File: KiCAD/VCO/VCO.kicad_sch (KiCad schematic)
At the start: 34 parts, among them Q1 NPN, T1 PNP, T2 NPN, U1 4069, U2 4069, U3 4069

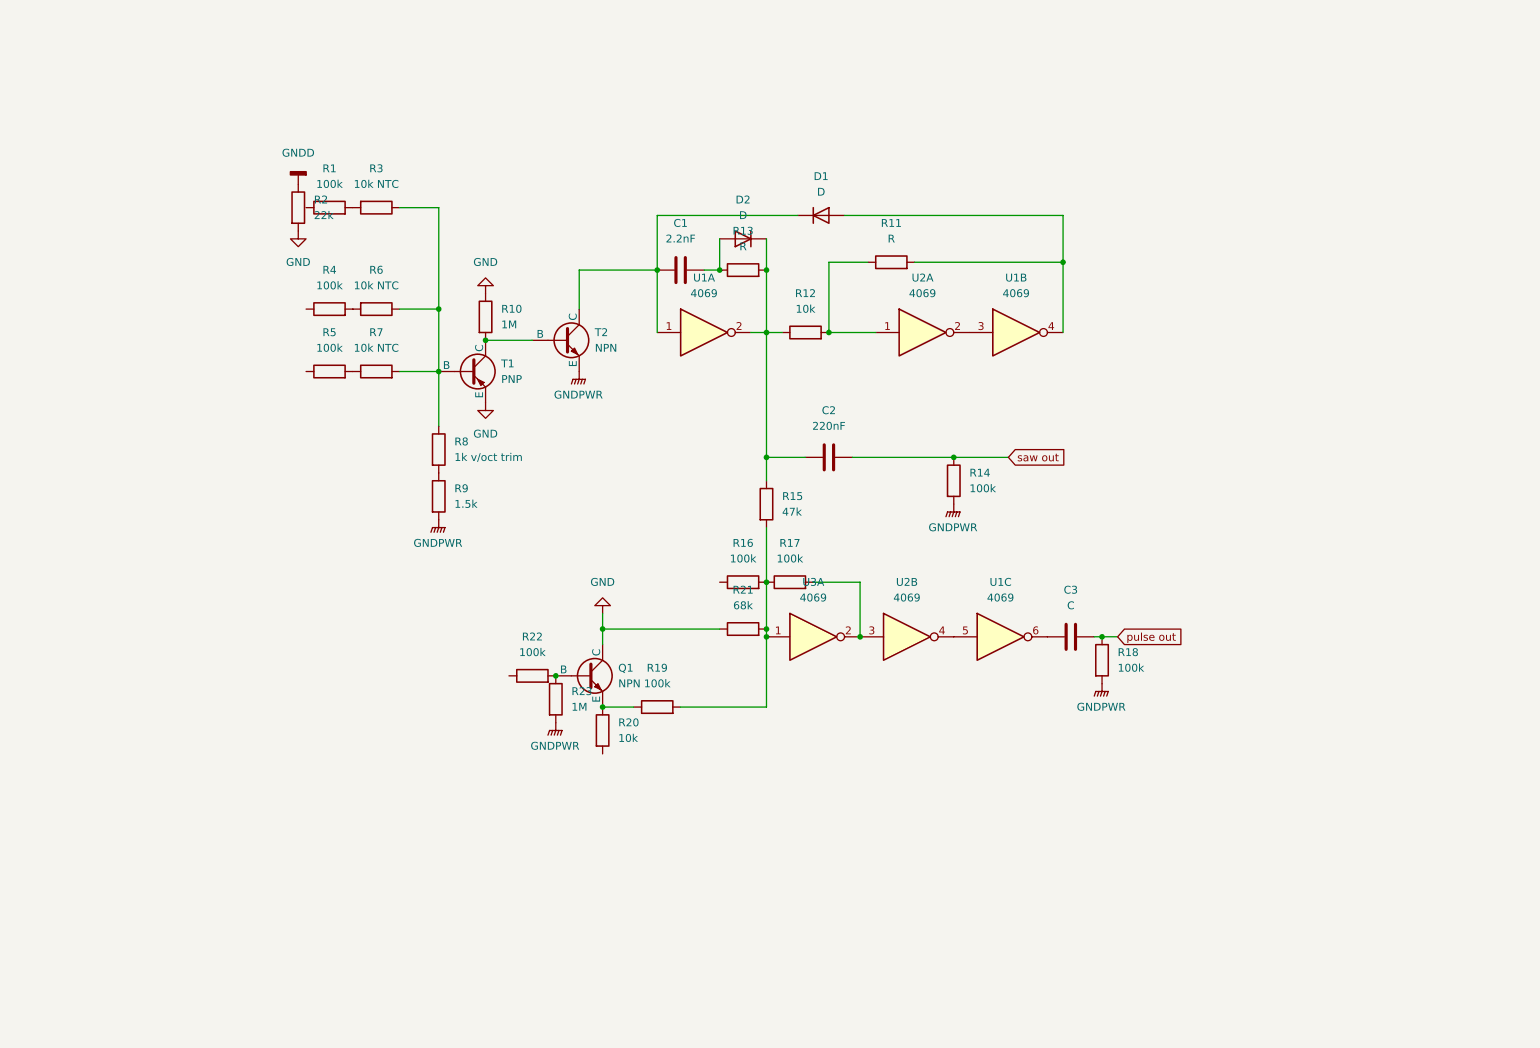
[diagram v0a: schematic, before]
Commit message: Add footprint library components.
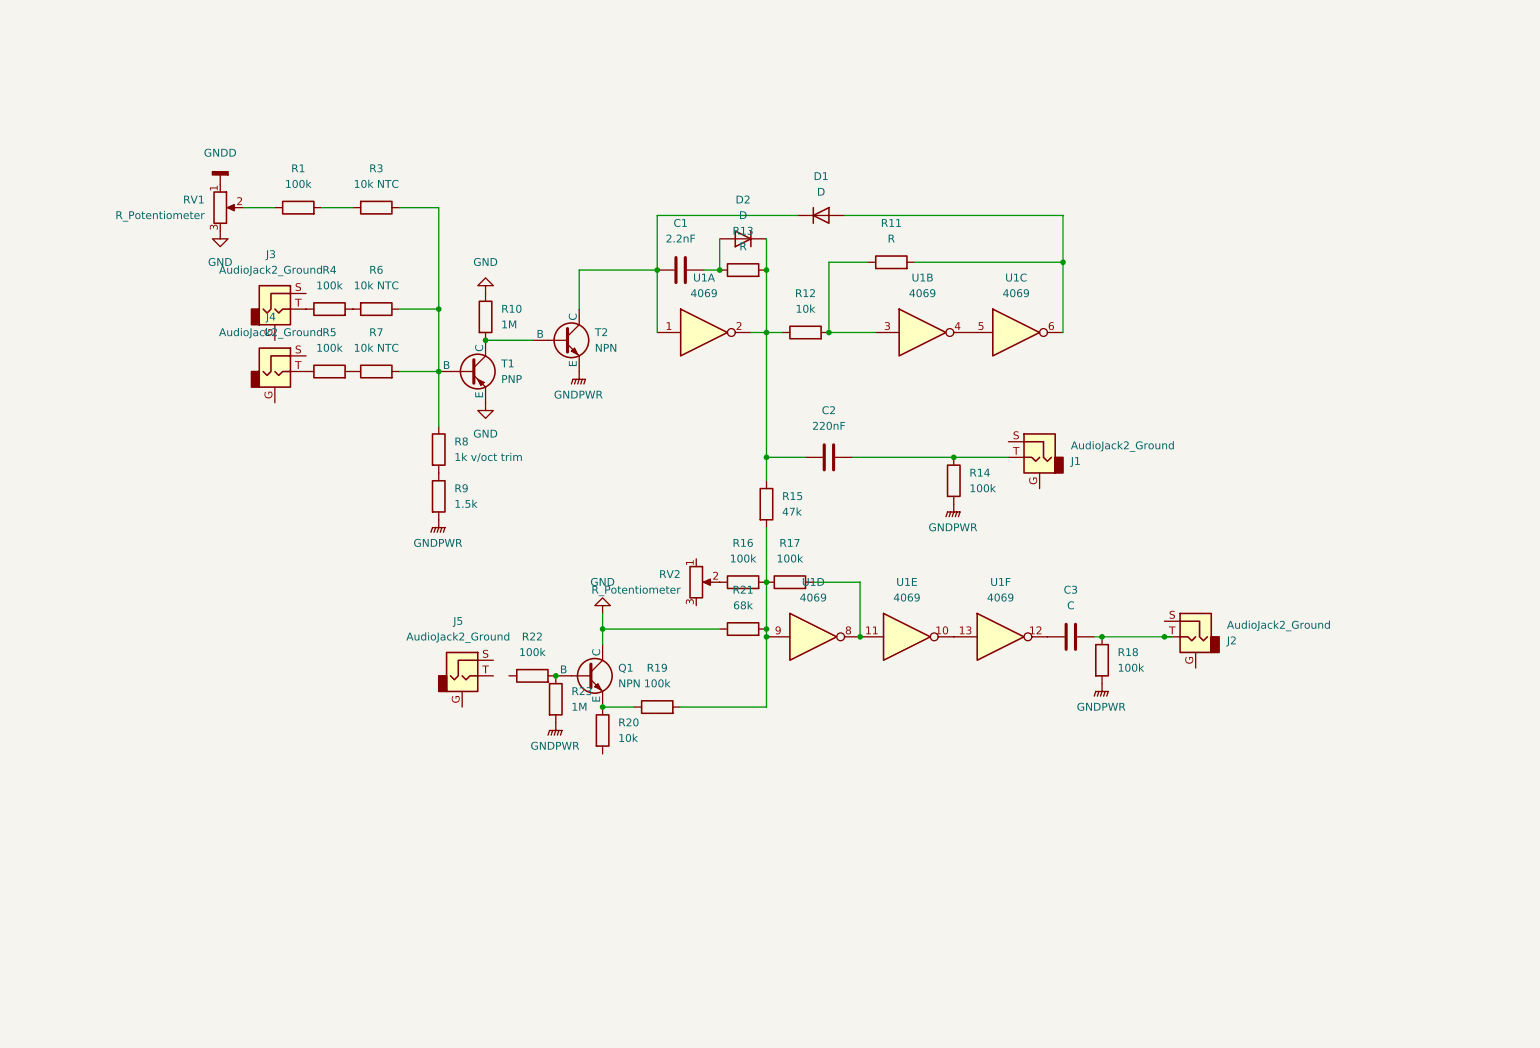
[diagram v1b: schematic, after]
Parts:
- removed R2: 22k, symbol Device:R
- added J1, J2, J3, J4, J5: AudioJack2_Ground, HackSynth:Jack_3.5mm, symbol HackSynth:AudioJack2_Ground
- added RV1, RV2: R_Potentiometer, HackSynth:Potentiometer_Alps_RK09K_Horizontal, symbol HackSynth:R_Potentiometer
- C1, C2, C3: footprint (none) -> Capacitor_THT:C_Disc_D5.0mm_W2.5mm_P2.50mm
- D1, D2: footprint (none) -> Diode_THT:D_5KPW_P12.70mm_Horizontal
- Q1: footprint (none) -> Package_TO_SOT_THT:TO-92L_Inline
- R1, R10, R11, R12, R13, R14, R15, R16, R17, R18, R19, R20, R21, R22, R23, R3, R4, R5, R6, R7, R8, R9: footprint (none) -> Resistor_THT:R_Axial_DIN0207_L6.3mm_D2.5mm_P7.62mm_Horizontal
- T1, T2: footprint (none) -> Package_TO_SOT_THT:TO-92_Inline
- U1: renamed from U3; footprint (none) -> Package_DIP:DIP-4_W7.62mm_LongPads
- U1: renamed from U2; footprint (none) -> Package_DIP:DIP-4_W7.62mm_LongPads
- U1: footprint (none) -> Package_DIP:DIP-4_W7.62mm_LongPads
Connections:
- net GND: now also RV1.3
- net GNDD: now also RV1.1
- net at R16.1: now also RV2.2
- net at R15.2, R16.2, R17.1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: now also U1.9; no longer U1.1
- net at C3.1: now also U1.12; no longer U1.6
- net at R5.1: now also J4.T
- net at D1.2 (A), R11.2: now also U1.6; no longer U1.4
- net at R11.1, R12.2: now also U1.3; no longer U1.1
- net at R4.1: now also J3.T
- net at R1.1: now also RV1.2
- net pulse out: no longer names the net of C3.2, R18.1
- net pulse out: now also J2.T
- net saw out: no longer names the net of C2.2, R14.1
- net saw out: now also J1.T
- new net: R17.2, U1.11, U1.8
- new net: U1.10, U1.13
- new net: U1.4, U1.5
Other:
- moved on the sheet: R1

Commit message: VCO and Power updates
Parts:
- removed R8: 1k v/oct trim, Resistor_THT:R_Axial_DIN0207_L6.3mm_D2.5mm_P7.62mm_Horizontal, symbol Device:R
- added RV3: R_Potentiometer_Trim 1k, symbol Device:R_Potentiometer_Trim
- C3: value C -> 220nF
- renumbered J3 to J1, J4 to J2, J5 to J3, J1 to J4, J2 to J5
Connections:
- net GNDD is gone; now on net GND: RV1.1
- net GNDPWR is gone; now on net GND: R14.2, R18.2, R23.2, R9.2, T2.3 (E)
- net GND: now also J1.G, J2.G, J3.G, J4.G, J5.G, RV2.3; no longer Q1.1 (C), R10.1, R21.1, RV1.3, T1.3 (E)
- net VDD: now reaches RV2.1
- net VDD: now also Q1.1 (C), R10.1, R21.1
- net at J3.T: now also R22.1
- net at R3.1, R6.1, R7.2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: now also RV3.1
- net at R9.1: now also RV3.2, RV3.3
- net VSS: now reaches R20.2
- net VSS: now also RV1.3, T1.3 (E)
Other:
- note added: "CV IN 1"
- note added: "CV IN 2"
- note added: "PULSE OUT"
- note added: "PW ADJUST"
- note added: "PWM"
- note added: "SAW OUT"
- note added: "V/OCT TRIM"
- moved on the sheet: C1, C2, C3, D1, D2, J1, J2, J3, J4, J5, Q1, R1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

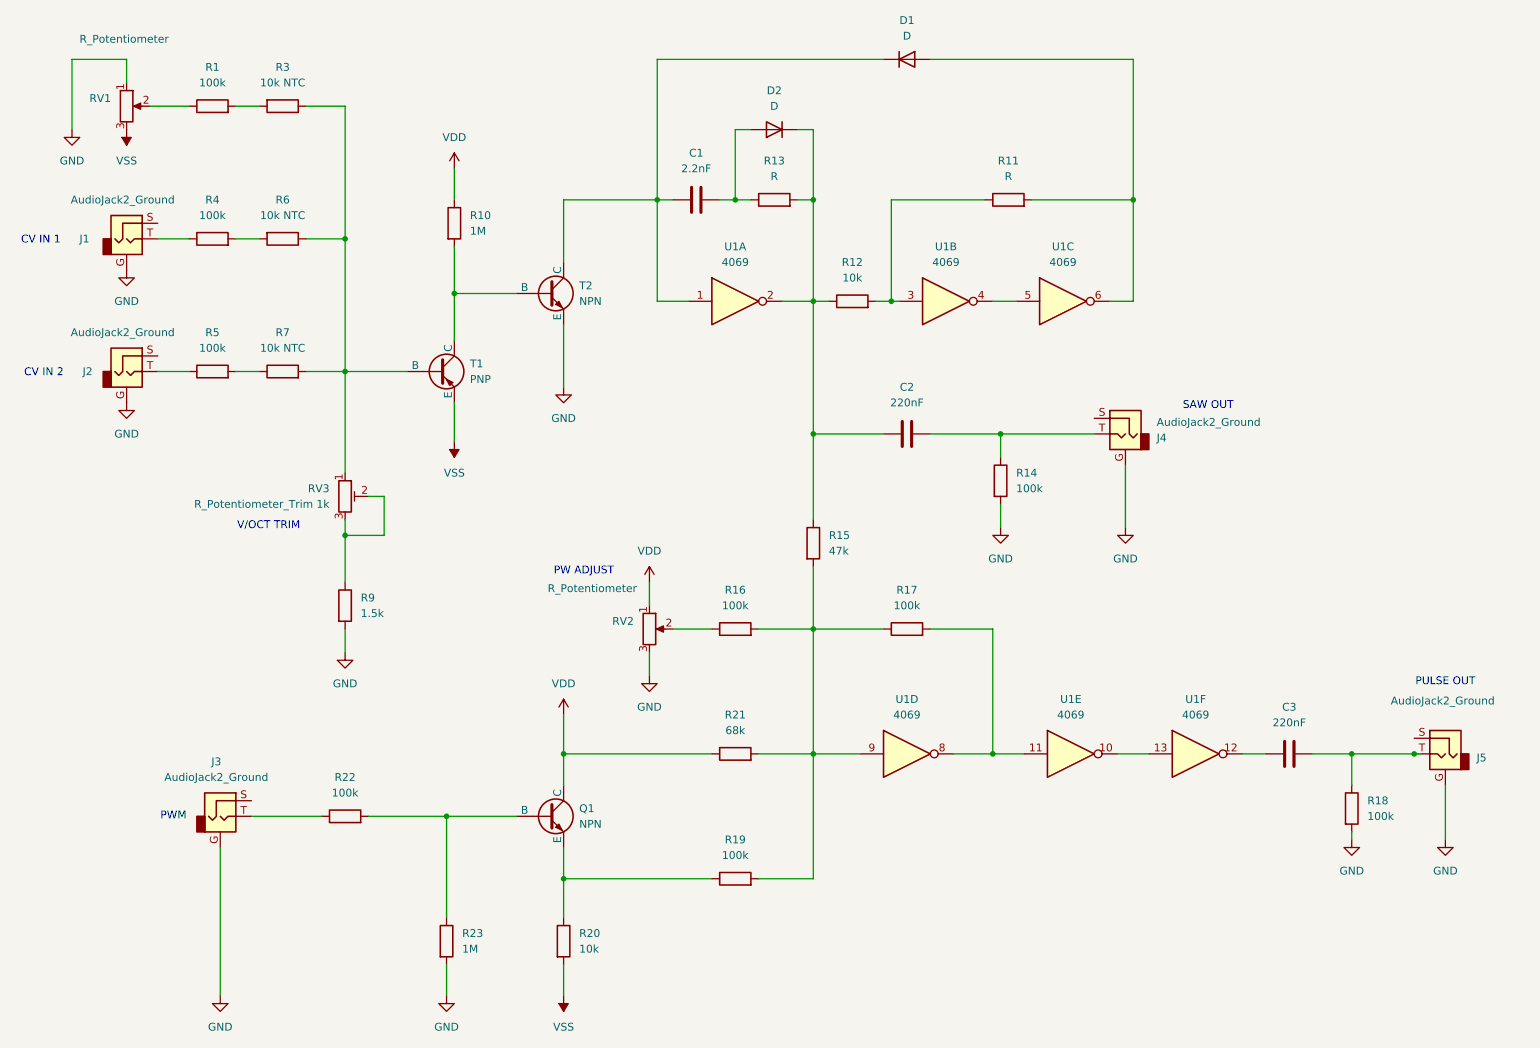
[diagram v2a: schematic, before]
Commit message: Power Schematic and Libraries
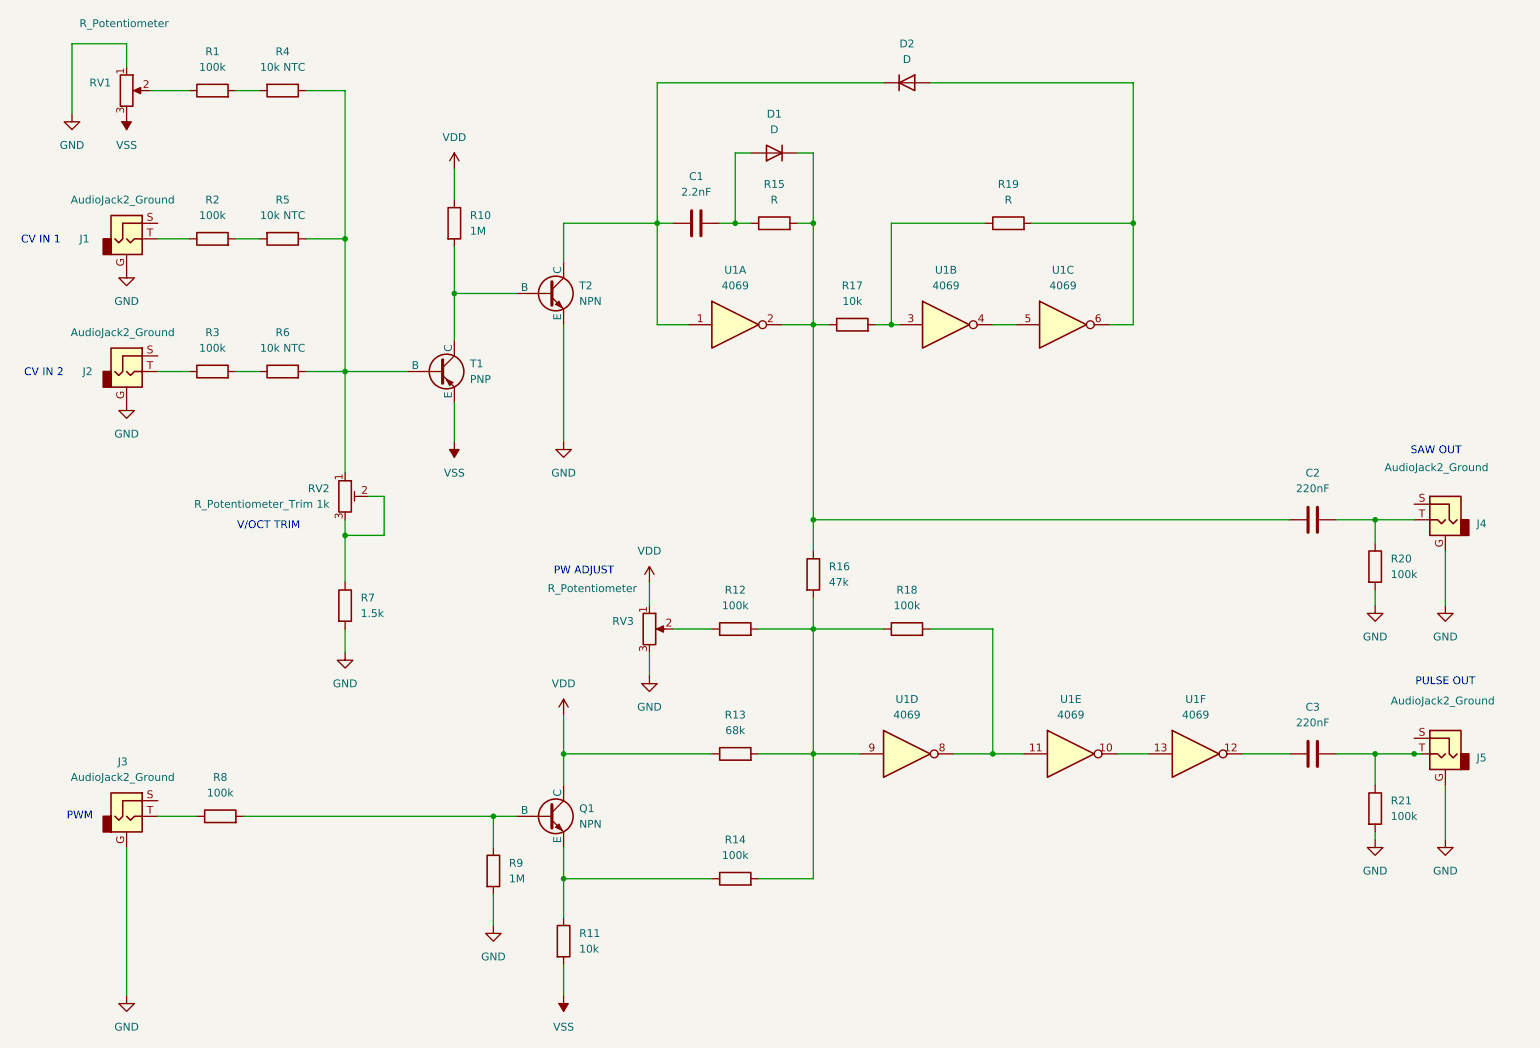
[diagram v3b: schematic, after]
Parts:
- D1: renamed from D2; footprint Diode_THT:D_5KPW_P12.70mm_Horizontal -> Diode_THT:D_A-405_P7.62mm_Horizontal
- D2: renamed from D1; footprint Diode_THT:D_5KPW_P12.70mm_Horizontal -> Diode_THT:D_A-405_P7.62mm_Horizontal
- U1: footprint Package_DIP:DIP-4_W7.62mm_LongPads -> Package_DIP:DIP-14_W7.62mm_LongPads
- renumbered R20 to R11, R16 to R12, R21 to R13, R19 to R14, R13 to R15, R15 to R16, R12 to R17, R17 to R18, R11 to R19, R4 to R2, R14 to R20, R18 to R21, R5 to R3, R3 to R4, R6 to R5, R7 to R6, R9 to R7, R22 to R8, R23 to R9, RV3 to RV2, RV2 to RV3
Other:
- moved on the sheet: C1, C2, C3, D1, D2, J3, J4, R1, R15, R16, R17, R19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

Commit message: VCA Schematic
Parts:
- J1: value AudioJack2_Ground -> CV IN 1
- J2: value AudioJack2_Ground -> CV IN 2
- J3: value AudioJack2_Ground -> PWM
- J4: value AudioJack2_Ground -> SAW OUT
- J5: value AudioJack2_Ground -> PULSE OUT
- RV2: footprint (none) -> HackSynth:TrimPot_Bourns_3339S_Horizontal
- RV3: value R_Potentiometer -> PW ADJUST
- T1, T2: footprint Package_TO_SOT_THT:TO-92_Inline -> HackSynth:TO-92_Inline - Handsolder
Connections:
- no-connect marks 0 -> 5
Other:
- note removed: "CV IN 1"
- note removed: "CV IN 2"
- note removed: "PULSE OUT"
- note removed: "PW ADJUST"
- note removed: "PWM"
- note removed: "SAW OUT"
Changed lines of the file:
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@@
 	(generator_version "9.0")
 	(paper "A4")
-	(text "CV IN 2"
-		(exclude_from_sim no)
-		(at 32.258 78.994 0)
-		(effects
-			(font
-				(size 1.27 1.27)
-			)
-		)
-	)
-	(text "PULSE OUT"
-		(exclude_from_sim no)
-		(at 260.35 129.286 0)
-		(effects
-			(font
-				(size 1.27 1.27)
-			)
-		)
-	)
-	(text "PWM"
-		(exclude_from_sim no)
-		(at 38.1 151.13 0)
-		(effects
-			(font
-				(size 1.27 1.27)
-			)
-		)
-	)
-	(text "PW ADJUST"
-		(exclude_from_sim no)
-		(at 120.142 111.252 0)
-		(effects
-			(font
-				(size 1.27 1.27)
-			)
-		)
-	)
 	(text "V/OCT TRIM"
 		(exclude_from_sim no)
@@
 		)
 	)
-	(text "SAW OUT"
-		(exclude_from_sim no)
-		(at 258.826 91.694 0)
-		(effects
-			(font
-				(size 1.27 1.27)
-			)
-		)
-	)
-	(text "CV IN 1"
-		(exclude_from_sim no)
-		(at 31.75 57.404 0)
-		(effects
-			(font
-				(size 1.27 1.27)
-			)
-		)
-	)
 	(junction
 		(at 81.28 57.15)
@@
 		(color 0 0 0 0)
 	)
+	(no_connect
+		(at 50.8 54.61)
+	)
+	(no_connect
+		(at 50.8 148.59)
+	)
+	(no_connect
+		(at 255.27 100.33)
+	)
+	(no_connect
+		(at 50.8 76.2)
+	)
+	(no_connect
+		(at 255.27 138.43)
+	)
 	(wire
 		(pts
@@
 			)
 		)
-		(property "Value" "R_Potentiometer"
+		(property "Value" "PW ADJUST"
 			(at 128.778 114.046 0)
 			(effects
@@
 			)
 		)
-		(property "Value" "AudioJack2_Ground"
+		(property "Value" "PWM"
 			(at 45.085 144.78 0)
 			(effects
@@
 			)
 		)
-		(property "Value" "AudioJack2_Ground"
+		(property "Value" "CV IN 2"
 			(at 45.085 72.39 0)
 			(effects
@@
 			)
 		)
-		(property "Value" "AudioJack2_Ground"
-			(at 250.444 94.3611 0)
+		(property "Value" "SAW OUT"
+			(at 256.032 95.504 0)
 			(effects
 				(font
@@
 			)
 		)
-		(property "Footprint" ""
+		(property "Footprint" "HackSynth:TrimPot_Bourns_3339S_Horizontal"
 			(at 81.28 99.06 0)
 			(effects
@@
 			)
 		)
-		(property "Footprint" "Package_TO_SOT_THT:TO-92_Inline"
+		(property "Footprint" "HackSynth:TO-92_Inline - Handsolder"
 			(at 132.08 78.74 0)
 			(effects
@@
 			)
 		)
-		(property "Value" "AudioJack2_Ground"
+		(property "Value" "CV IN 1"
 			(at 45.085 50.8 0)
 			(effects
@@
 			)
 		)
-		(property "Value" "AudioJack2_Ground"
-			(at 251.46 132.334 0)
+		(property "Value" "PULSE OUT"
+			(at 254.762 132.842 0)
 			(effects
 				(font
@@
 			)
 		)
-		(property "Footprint" "Package_TO_SOT_THT:TO-92_Inline"
+		(property "Footprint" "HackSynth:TO-92_Inline - Handsolder"
 			(at 177.8 66.04 0)
 			(effects

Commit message: Notes
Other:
- note added: "Check Pin Order on Footprint"
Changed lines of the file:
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@@
 	(generator_version "9.0")
 	(paper "A4")
+	(text "Check Pin Order on Footprint"
+		(exclude_from_sim no)
+		(at 107.696 72.39 0)
+		(effects
+			(font
+				(size 2 2)
+			)
+		)
+	)
 	(text "V/OCT TRIM"
 		(exclude_from_sim no)

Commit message: Mid VCO pcb session.
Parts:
- added J6, J7: Conn_01x03_Pin, HackSynth:JST_PH_S3B-PH-K_1x03_P2.00mm_Horizontal, symbol Connector:Conn_01x03_Pin
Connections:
- net GND: now also J6.1 (Pin_1), J7.1 (Pin_1)
- net VDD: now also J6.2 (Pin_2), J7.2 (Pin_2)
- net VSS: now also J6.3 (Pin_3), J7.3 (Pin_3)

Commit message: Minor VCO update
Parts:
- added unit 7 of U1
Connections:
- net VDD: now also U1.14 (VDD)
- net VSS: now also U1.7 (VSS)
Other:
- moved on the sheet: J6, J7

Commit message: Reapply VCO pcb layout changes.
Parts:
- R4, R5, R6: footprint Resistor_THT:R_Axial_DIN0207_L6.3mm_D2.5mm_P7.62mm_Horizontal -> Resistor_THT:R_Axial_DIN0207_L6.3mm_D2.5mm_P2.54mm_Vertical
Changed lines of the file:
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@@
 			)
 		)
-		(property "Footprint" "Resistor_THT:R_Axial_DIN0207_L6.3mm_D2.5mm_P7.62mm_Horizontal"
+		(property "Footprint" "Resistor_THT:R_Axial_DIN0207_L6.3mm_D2.5mm_P2.54mm_Vertical"
 			(at 71.12 31.242 90)
 			(effects
@@
 			)
 		)
-		(property "Footprint" "Resistor_THT:R_Axial_DIN0207_L6.3mm_D2.5mm_P7.62mm_Horizontal"
+		(property "Footprint" "Resistor_THT:R_Axial_DIN0207_L6.3mm_D2.5mm_P2.54mm_Vertical"
 			(at 71.12 55.372 90)
 			(effects
@@
 			)
 		)
-		(property "Footprint" "Resistor_THT:R_Axial_DIN0207_L6.3mm_D2.5mm_P7.62mm_Horizontal"
+		(property "Footprint" "Resistor_THT:R_Axial_DIN0207_L6.3mm_D2.5mm_P2.54mm_Vertical"
 			(at 71.12 80.518 90)
 			(effects
